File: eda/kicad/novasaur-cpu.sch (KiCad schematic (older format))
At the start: 29 parts, among them U14 27C020, U15 AS6C4008, U16 74F574, U17 74F163, U18 74F163, U19 74F541, U20 74F574, U21 74F574, U22 74F257, U23 74F574, U24 74F574, U25 74F574, U26 74F574, U27 74F244, U27 74F541

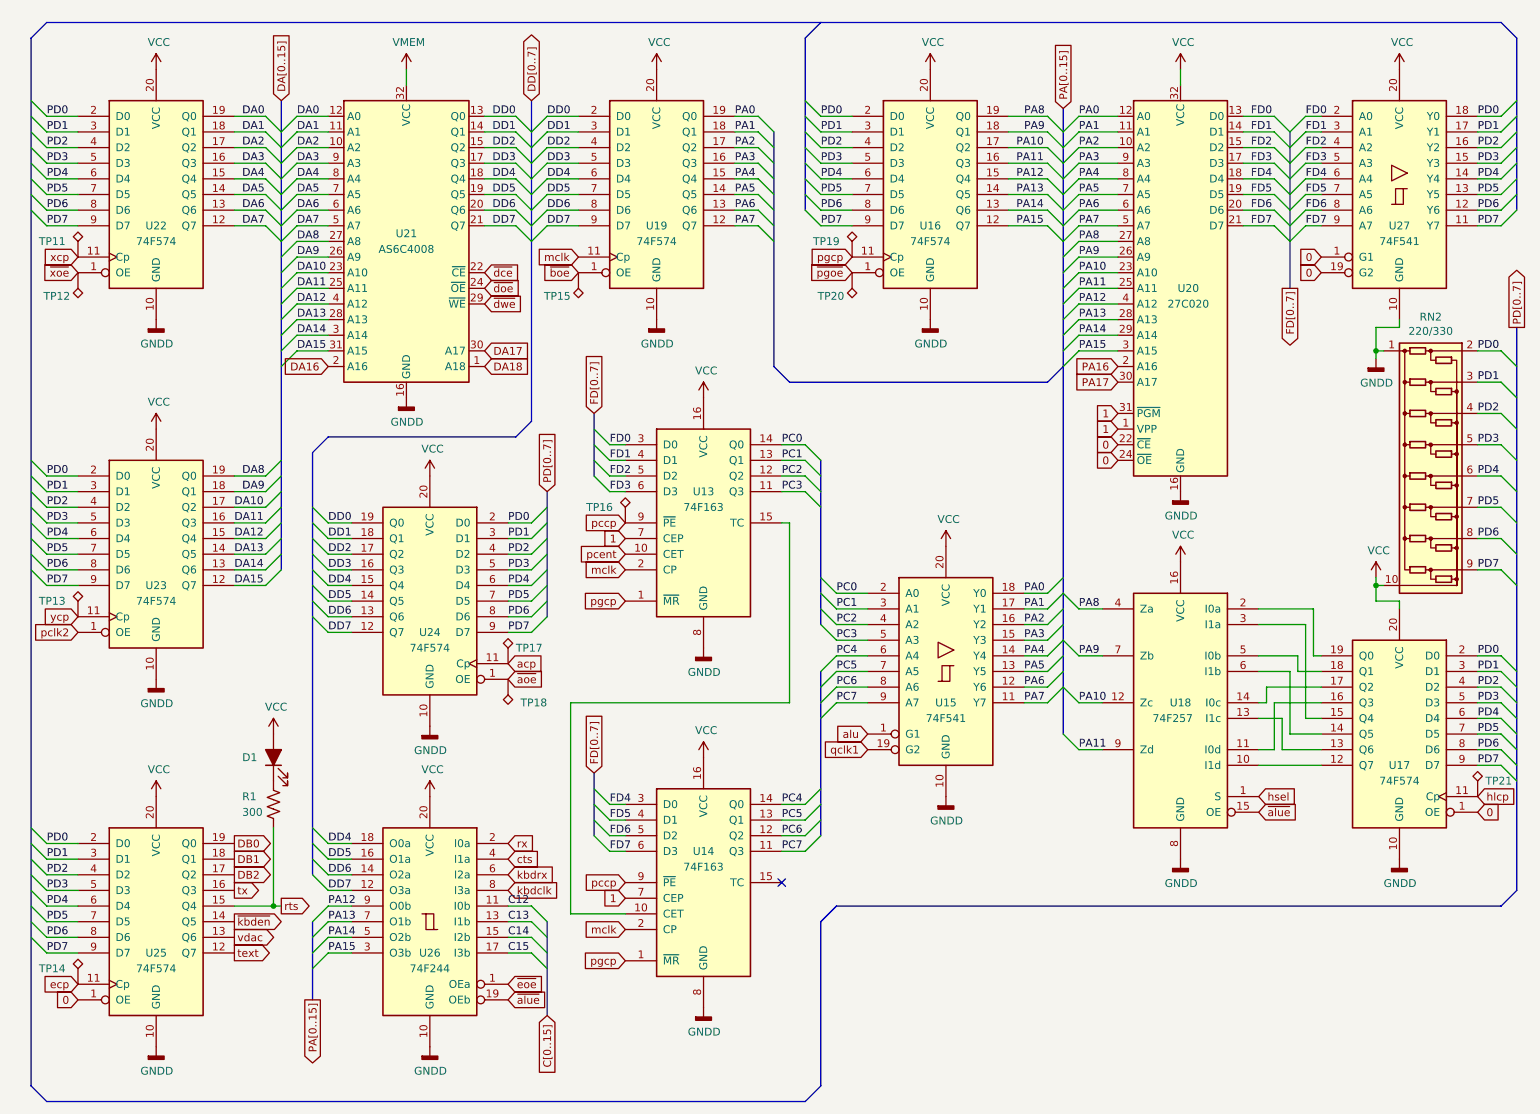
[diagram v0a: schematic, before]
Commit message: add TVS diode ESD protection
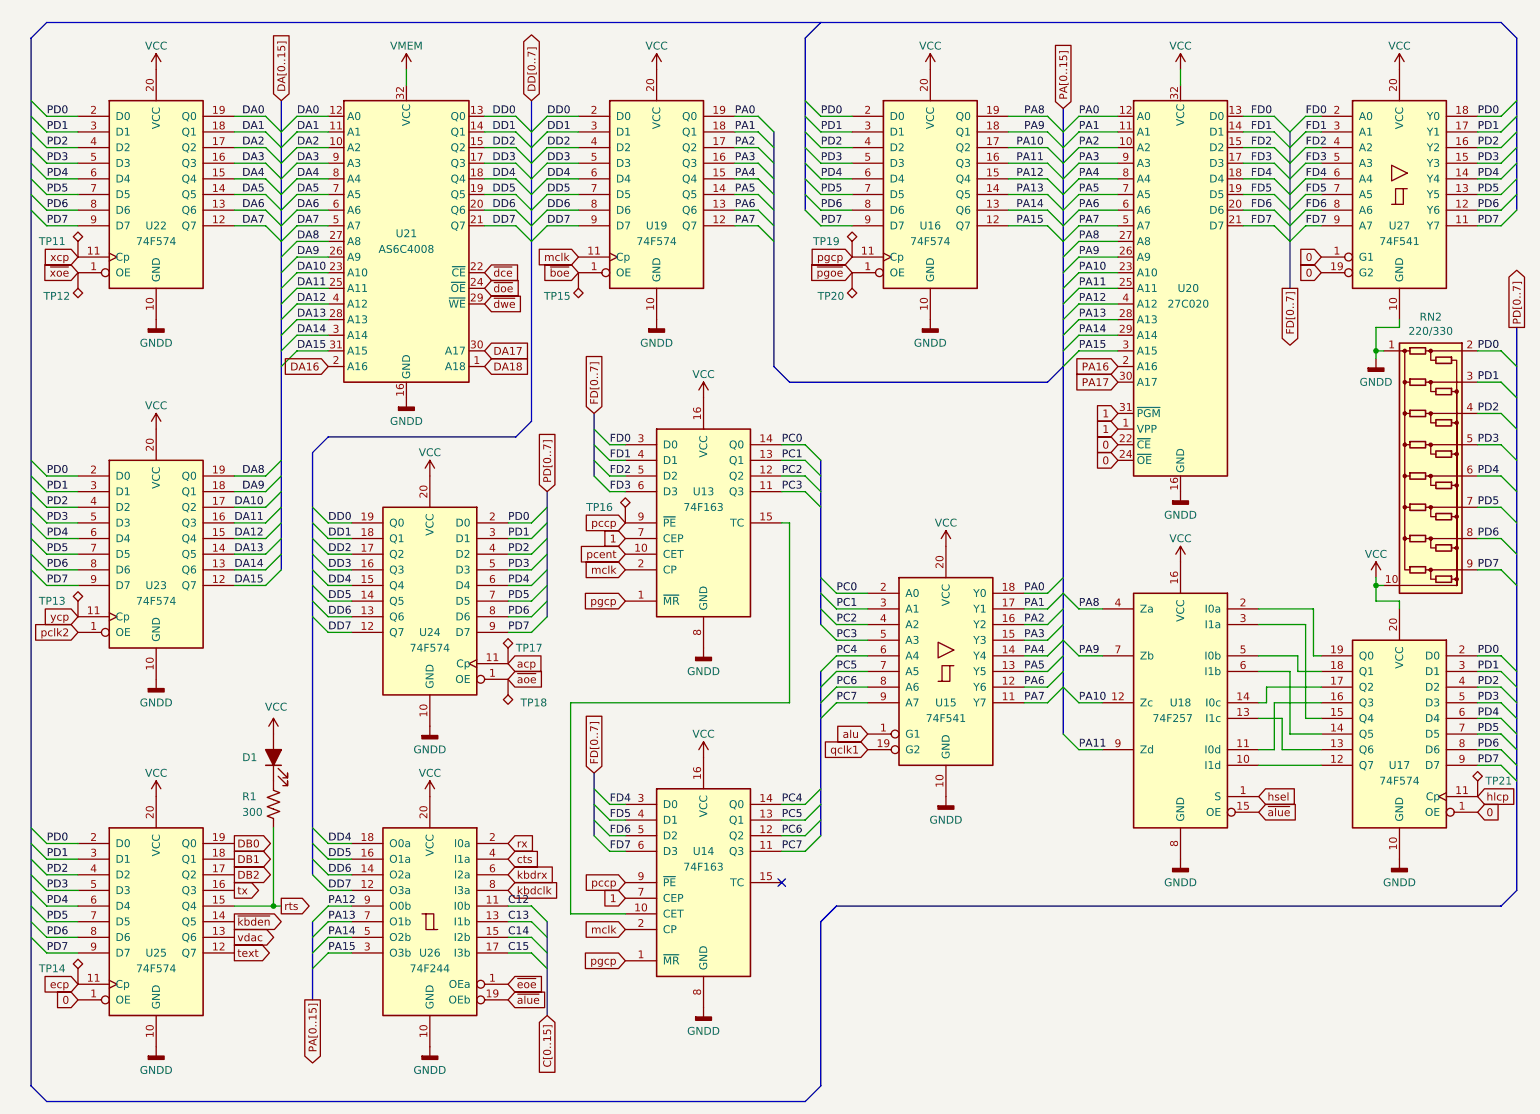
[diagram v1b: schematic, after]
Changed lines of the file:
@@
 Sheet 2 4
 Title "Central Processing Unit"
-Date "2021-06-06"
-Rev "1.9"
+Date "2021-07-10"
+Rev "1.10"
 Comp ""
 Comment1 "(c) Solid State Machines 2021"
@@
 AR Path="/5DA1E9BA/5DAE3510" Ref="#PWR0119"  Part="1"
 F 0 "#PWR0119" H 8100 5900 50  0001 C CNN
-F 1 "GNDD" H 8104 5995 50  0000 C CNN
+F 1 "GNDD" H 8100 6000 50  0000 C CNN
 F 2 "" H 8100 6150 50  0001 C CNN
 F 3 "" H 8100 6150 50  0001 C CNN
@@
 AR Path="/5DA1E9BA/5DAE3651" Ref="#PWR0129"  Part="1"
 F 0 "#PWR0129" H 8100 950 50  0001 C CNN
-F 1 "VCC" H 8117 1273 50  0000 C CNN
+F 1 "VCC" H 8100 1250 50  0000 C CNN
 F 2 "" H 8100 1100 50  0001 C CNN
 F 3 "" H 8100 1100 50  0001 C CNN
@@
 AR Path="/5DA1E9BA/5DAE3675" Ref="#PWR0133"  Part="1"
 F 0 "#PWR0133" H 8100 4100 50  0001 C CNN
-F 1 "VCC" H 8117 4423 50  0000 C CNN
+F 1 "VCC" H 8100 4400 50  0000 C CNN
 F 2 "" H 8100 4250 50  0001 C CNN
 F 3 "" H 8100 4250 50  0001 C CNN
@@
 AR Path="/5DA1E9BA/5DAE34BA" Ref="#PWR0135"  Part="1"
 F 0 "#PWR0135" H 8100 3550 50  0001 C CNN
-F 1 "GNDD" H 8104 3645 50  0000 C CNN
+F 1 "GNDD" H 8100 3650 50  0000 C CNN
 F 2 "" H 8100 3800 50  0001 C CNN
 F 3 "" H 8100 3800 50  0001 C CNN
@@
 AR Path="/5DA1E9BA/5DAE368B" Ref="#PWR0136"  Part="1"
 F 0 "#PWR0136" H 9500 5900 50  0001 C CNN
-F 1 "GNDD" H 9504 5995 50  0000 C CNN
+F 1 "GNDD" H 9500 6000 50  0000 C CNN
 F 2 "" H 9500 6150 50  0001 C CNN
 F 3 "" H 9500 6150 50  0001 C CNN
@@
 AR Path="/5DA1E9BA/5DAE3681" Ref="#PWR0137"  Part="1"
 F 0 "#PWR0137" H 9350 4200 50  0001 C CNN
-F 1 "VCC" H 9367 4523 50  0000 C CNN
+F 1 "VCC" H 9350 4500 50  0000 C CNN
 F 2 "" H 9350 4350 50  0001 C CNN
 F 3 "" H 9350 4350 50  0001 C CNN
@@
 AR Path="/5DA1E9BA/5DAE35F1" Ref="#PWR0120"  Part="1"
 F 0 "#PWR0120" H 6500 2450 50  0001 C CNN
-F 1 "GNDD" H 6504 2545 50  0000 C CNN
+F 1 "GNDD" H 6500 2550 50  0000 C CNN
 F 2 "" H 6500 2700 50  0001 C CNN
 F 3 "" H 6500 2700 50  0001 C CNN
@@
 AR Path="/5DA1E9BA/5DAE367B" Ref="#PWR0132"  Part="1"
 F 0 "#PWR0132" H 6500 950 50  0001 C CNN
-F 1 "VCC" H 6517 1273 50  0000 C CNN
+F 1 "VCC" H 6500 1250 50  0000 C CNN
 F 2 "" H 6500 1100 50  0001 C CNN
 F 3 "" H 6500 1100 50  0001 C CNN
@@
 AR Path="/5DA1E9BA/5DAE34AE" Ref="#PWR0141"  Part="1"
 F 0 "#PWR0141" H 3300 7100 50  0001 C CNN
-F 1 "GNDD" H 3304 7195 50  0000 C CNN
+F 1 "GNDD" H 3300 7200 50  0000 C CNN
 F 2 "" H 3300 7350 50  0001 C CNN
 F 3 "" H 3300 7350 50  0001 C CNN
@@
 AR Path="/5DA1E9BA/5DAE3669" Ref="#PWR0140"  Part="1"
 F 0 "#PWR0140" H 3300 5600 50  0001 C CNN
-F 1 "VCC" H 3317 5923 50  0000 C CNN
+F 1 "VCC" H 3300 5900 50  0000 C CNN
 F 2 "" H 3300 5750 50  0001 C CNN
 F 3 "" H 3300 5750 50  0001 C CNN
@@
 AR Path="/5DA1E9BA/5F43317A" Ref="#PWR0139"  Part="1"
 F 0 "#PWR0139" H 3300 3550 50  0001 C CNN
-F 1 "VCC" H 3317 3873 50  0000 C CNN
+F 1 "VCC" H 3300 3850 50  0000 C CNN
 F 2 "" H 3300 3700 50  0001 C CNN
 F 3 "" H 3300 3700 50  0001 C CNN
@@
 AR Path="/5DA1E9BA/5F008C47" Ref="#PWR0138"  Part="1"
 F 0 "#PWR0138" H 3300 5050 50  0001 C CNN
-F 1 "GNDD" H 3304 5145 50  0000 C CNN
+F 1 "GNDD" H 3300 5150 50  0000 C CNN
 F 2 "" H 3300 5300 50  0001 C CNN
 F 3 "" H 3300 5300 50  0001 C CNN
@@
 AR Path="/5DA1E9BA/5DAE3645" Ref="#PWR0128"  Part="1"
 F 0 "#PWR0128" H 4750 950 50  0001 C CNN
-F 1 "VCC" H 4767 1273 50  0000 C CNN
+F 1 "VCC" H 4750 1250 50  0000 C CNN
 F 2 "" H 4750 1100 50  0001 C CNN
 F 3 "" H 4750 1100 50  0001 C CNN
@@
 AR Path="/5DA1E9BA/5DAE3639" Ref="#PWR0127"  Part="1"
 F 0 "#PWR0127" H 1550 950 50  0001 C CNN
-F 1 "VCC" H 1567 1273 50  0000 C CNN
+F 1 "VCC" H 1550 1250 50  0000 C CNN
 F 2 "" H 1550 1100 50  0001 C CNN
 F 3 "" H 1550 1100 50  0001 C CNN
@@
 AR Path="/5DA1E9BA/5DAE362D" Ref="#PWR0125"  Part="1"
 F 0 "#PWR0125" H 5050 5350 50  0001 C CNN
-F 1 "VCC" H 5067 5673 50  0000 C CNN
+F 1 "VCC" H 5050 5650 50  0000 C CNN
 F 2 "" H 5050 5500 50  0001 C CNN
 F 3 "" H 5050 5500 50  0001 C CNN
@@
 AR Path="/5DA1E9BA/5DAE3623" Ref="#PWR0124"  Part="1"
 F 0 "#PWR0124" H 6600 4000 50  0001 C CNN
-F 1 "VCC" H 6617 4323 50  0000 C CNN
+F 1 "VCC" H 6600 4300 50  0000 C CNN
 F 2 "" H 6600 4150 50  0001 C CNN
 F 3 "" H 6600 4150 50  0001 C CNN
@@
 AR Path="/5DA1E9BA/5DAE3603" Ref="#PWR0123"  Part="1"
 F 0 "#PWR0123" H 3150 2950 50  0001 C CNN
-F 1 "GNDD" H 3154 3045 50  0000 C CNN
+F 1 "GNDD" H 3150 3050 50  0000 C CNN
 F 2 "" H 3150 3200 50  0001 C CNN
 F 3 "" H 3150 3200 50  0001 C CNN
@@
 AR Path="/5DA1E9BA/5DAE35FD" Ref="#PWR0122"  Part="1"
 F 0 "#PWR0122" H 1550 2450 50  0001 C CNN
-F 1 "GNDD" H 1554 2545 50  0000 C CNN
+F 1 "GNDD" H 1550 2550 50  0000 C CNN
 F 2 "" H 1550 2700 50  0001 C CNN
 F 3 "" H 1550 2700 50  0001 C CNN
@@
 AR Path="/5DA1E9BA/5DAE346C" Ref="#PWR0118"  Part="1"
 F 0 "#PWR0118" H 4750 2450 50  0001 C CNN
-F 1 "GNDD" H 4754 2545 50  0000 C CNN
+F 1 "GNDD" H 4750 2550 50  0000 C CNN
 F 2 "" H 4750 2700 50  0001 C CNN
 F 3 "" H 4750 2700 50  0001 C CNN
@@
 AR Path="/5DA1E9BA/5DAE345E" Ref="#PWR0116"  Part="1"
 F 0 "#PWR0116" H 6600 5500 50  0001 C CNN
-F 1 "GNDD" H 6604 5595 50  0000 C CNN
+F 1 "GNDD" H 6600 5600 50  0000 C CNN
 F 2 "" H 6600 5750 50  0001 C CNN
 F 3 "" H 6600 5750 50  0001 C CNN
@@
 AR Path="/5DA1E9BA/5DAE3464" Ref="#PWR0117"  Part="1"
 F 0 "#PWR0117" H 5050 6850 50  0001 C CNN
-F 1 "GNDD" H 5054 6945 50  0000 C CNN
+F 1 "GNDD" H 5050 6950 50  0000 C CNN
 F 2 "" H 5050 7100 50  0001 C CNN
 F 3 "" H 5050 7100 50  0001 C CNN
@@
 AR Path="/5DA1E9BA/5DA9E243" Ref="#PWR0170"  Part="1"
 F 0 "#PWR0170" H 9500 950 50  0001 C CNN
-F 1 "VCC" H 9517 1273 50  0000 C CNN
+F 1 "VCC" H 9500 1250 50  0000 C CNN
 F 2 "" H 9500 1100 50  0001 C CNN
 F 3 "" H 9500 1100 50  0001 C CNN
@@
 AR Path="/5DA1E9BA/5DAE3458" Ref="#PWR0115"  Part="1"
 F 0 "#PWR0115" H 5050 4550 50  0001 C CNN
-F 1 "GNDD" H 5054 4645 50  0000 C CNN
+F 1 "GNDD" H 5050 4650 50  0000 C CNN
 F 2 "" H 5050 4800 50  0001 C CNN
 F 3 "" H 5050 4800 50  0001 C CNN
@@
 AR Path="/5DA1E9BA/5DAE3633" Ref="#PWR0126"  Part="1"
 F 0 "#PWR0126" H 5050 3050 50  0001 C CNN
-F 1 "VCC" H 5067 3373 50  0000 C CNN
+F 1 "VCC" H 5050 3350 50  0000 C CNN
 F 2 "" H 5050 3200 50  0001 C CNN
 F 3 "" H 5050 3200 50  0001 C CNN
@@
 AR Path="/5DA1E9BA/5DC7127C" Ref="#PWR0190"  Part="1"
 F 0 "#PWR0190" H 9350 2700 50  0001 C CNN
-F 1 "GNDD" H 9354 2795 50  0000 C CNN
+F 1 "GNDD" H 9350 2800 50  0000 C CNN
 F 2 "" H 9350 2950 50  0001 C CNN
 F 3 "" H 9350 2950 50  0001 C CNN
@@
 AR Path="/5DA1E9BA/5DAE3657" Ref="#PWR0130"  Part="1"
 F 0 "#PWR0130" H 1550 5600 50  0001 C CNN
-F 1 "VCC" H 1567 5923 50  0000 C CNN
+F 1 "VCC" H 1550 5900 50  0000 C CNN
 F 2 "" H 1550 5750 50  0001 C CNN
 F 3 "" H 1550 5750 50  0001 C CNN
@@
 AR Path="/5DA1E9BA/5DAE35E5" Ref="#PWR0134"  Part="1"
 F 0 "#PWR0134" H 1550 7100 50  0001 C CNN
-F 1 "GNDD" H 1554 7195 50  0000 C CNN
+F 1 "GNDD" H 1550 7200 50  0000 C CNN
 F 2 "" H 1550 7350 50  0001 C CNN
 F 3 "" H 1550 7350 50  0001 C CNN
@@
 AR Path="/5DA1E9BA/5DAE365D" Ref="#PWR0131"  Part="1"
 F 0 "#PWR0131" H 1550 3250 50  0001 C CNN
-F 1 "VCC" H 1567 3573 50  0000 C CNN
+F 1 "VCC" H 1550 3550 50  0000 C CNN
 F 2 "" H 1550 3400 50  0001 C CNN
 F 3 "" H 1550 3400 50  0001 C CNN
@@
 AR Path="/5DA1E9BA/5DAE35F7" Ref="#PWR0121"  Part="1"
 F 0 "#PWR0121" H 1550 4750 50  0001 C CNN
-F 1 "GNDD" H 1554 4845 50  0000 C CNN
+F 1 "GNDD" H 1550 4850 50  0000 C CNN
 F 2 "" H 1550 5000 50  0001 C CNN
 F 3 "" H 1550 5000 50  0001 C CNN
@@
 P 3150 1100
 F 0 "#PWR0142" H 3150 950 50  0001 C CNN
-F 1 "VMEM" H 3165 1273 50  0000 C CNN
+F 1 "VMEM" H 3150 1250 50  0000 C CNN
 F 2 "" H 3150 1100 50  0001 C CNN
 F 3 "" H 3150 1100 50  0001 C CNN

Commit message: remove 6v regulator go back to rev.1 do not collect 00
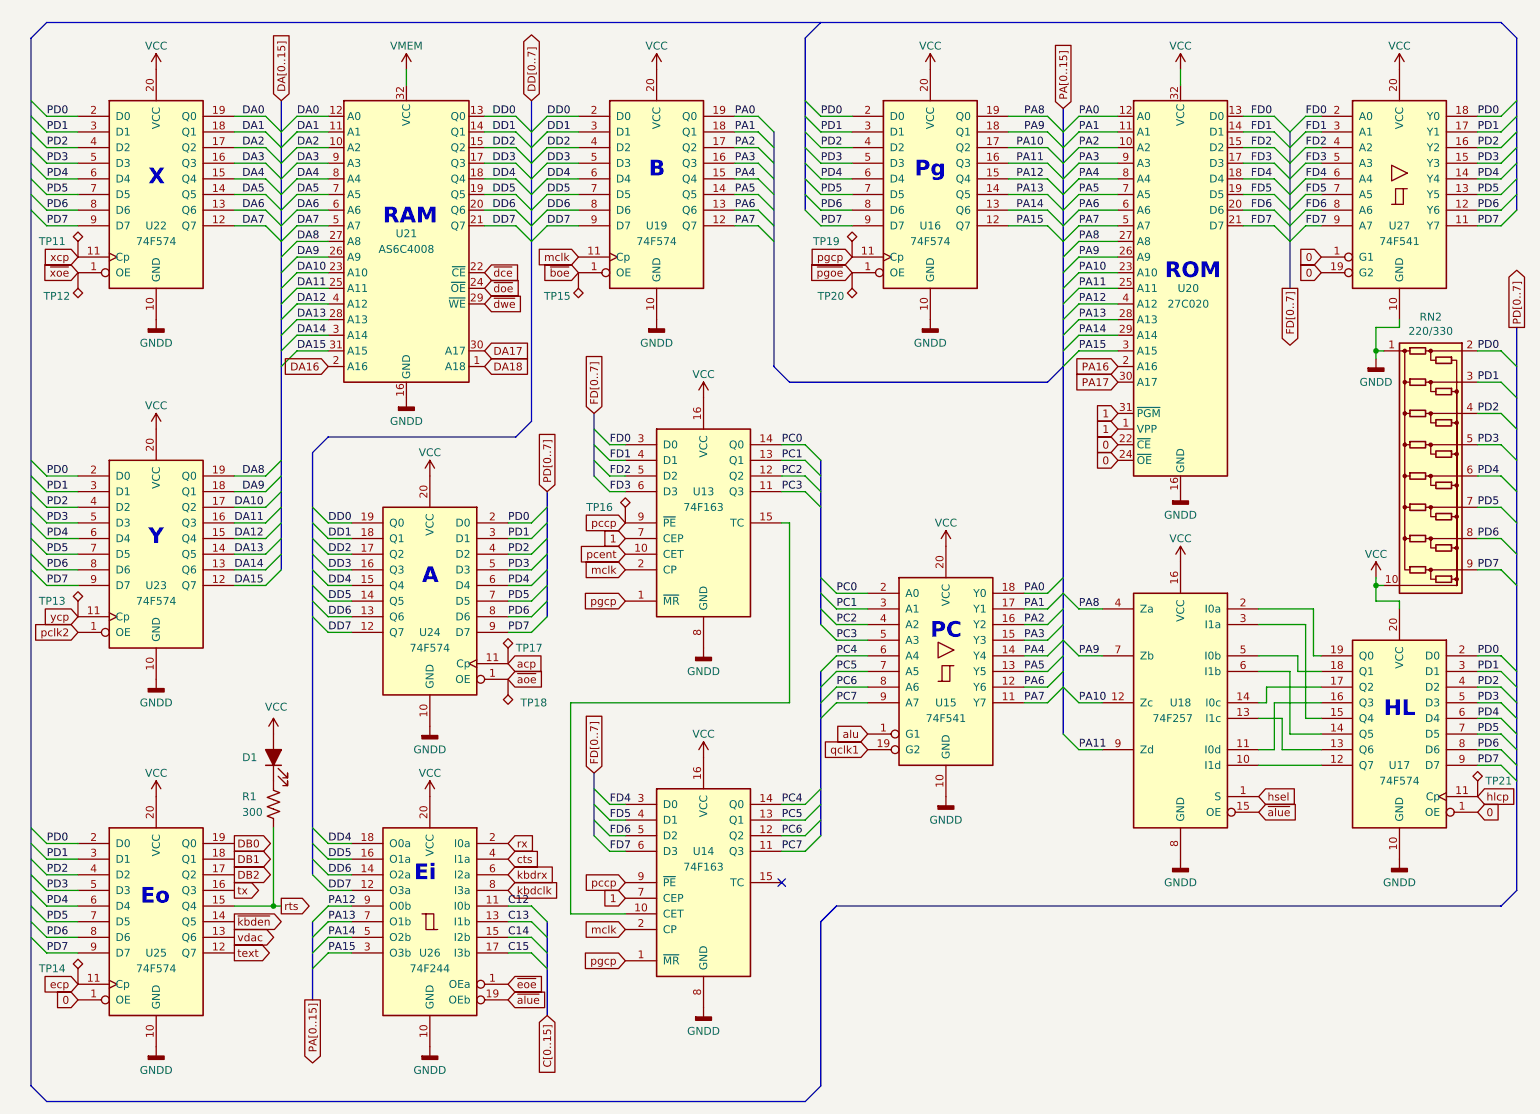
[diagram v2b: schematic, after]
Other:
- note added: "A"
- note added: "B"
- note added: "Ei"
- note added: "Eo"
- note added: "HL"
- note added: "PC"
- note added: "Pg"
- note added: "RAM"
- note added: "ROM"
- note added: "X"
- note added: "Y"
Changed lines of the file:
@@
 Sheet 2 4
 Title "Central Processing Unit"
-Date "2021-07-10"
+Date "2021-08-01"
 Rev "1.10"
 Comp ""
@@
 	1    0    0    -1
 $EndComp
+Text Notes 9400 5250 0    100  ~ 20
+HL
+Text Notes 3250 4400 0    100  ~ 20
+A
+Text Notes 1500 1850 0    100  ~ 20
+X
+Text Notes 1500 4150 0    100  ~ 20
+Y
+Text Notes 1450 6450 0    100  ~ 20
+Eo
+Text Notes 3200 6300 0    100  ~ 20
+Ei
+Text Notes 6500 4750 0    100  ~ 20
+PC
+Text Notes 6400 1800 0    100  ~ 20
+Pg
+Text Notes 4700 1800 0    100  ~ 20
+B
+Text Notes 8000 2450 0    100  ~ 20
+ROM
+Text Notes 3000 2100 0    100  ~ 20
+RAM
 Wire Bus Line
 	850  800  10150 800

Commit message: Rev. 10 with 5v PSU
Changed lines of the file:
@@
 Sheet 2 4
 Title "Central Processing Unit"
-Date "2021-08-01"
+Date "2021-09-02"
 Rev "1.10"
 Comp ""
@@
 	1    0    0    -1
 $EndComp
-Text Notes 9400 5250 0    100  ~ 20
+Text Notes 9400 5250 0    100  ~ 0
 HL
-Text Notes 3250 4400 0    100  ~ 20
+Text Notes 3250 4400 0    100  ~ 0
 A
-Text Notes 1500 1850 0    100  ~ 20
+Text Notes 1500 1850 0    100  ~ 0
 X
-Text Notes 1500 4150 0    100  ~ 20
+Text Notes 1500 4150 0    100  ~ 0
 Y
-Text Notes 1450 6450 0    100  ~ 20
+Text Notes 1450 6450 0    100  ~ 0
 Eo
-Text Notes 3200 6300 0    100  ~ 20
+Text Notes 3250 6450 0    100  ~ 0
 Ei
-Text Notes 6500 4750 0    100  ~ 20
+Text Notes 6500 4750 0    100  ~ 0
 PC
-Text Notes 6400 1800 0    100  ~ 20
+Text Notes 6400 1800 0    100  ~ 0
 Pg
-Text Notes 4700 1800 0    100  ~ 20
+Text Notes 4700 1800 0    100  ~ 0
 B
-Text Notes 8000 2450 0    100  ~ 20
+Text Notes 7950 1800 0    100  ~ 0
 ROM
-Text Notes 3000 2100 0    100  ~ 20
+Text Notes 3000 1850 0    100  ~ 0
 RAM
 Wire Bus Line
